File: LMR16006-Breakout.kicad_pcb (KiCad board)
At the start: 2 copper layers, 21 x 21 mm, 16 parts, among them P1 CONN_01X04, U1 LMR16006

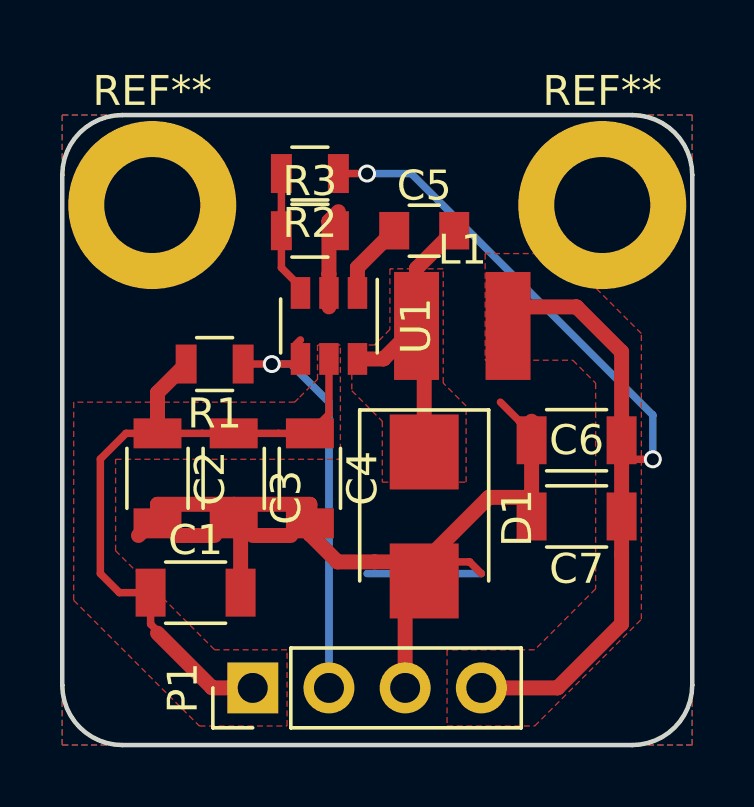
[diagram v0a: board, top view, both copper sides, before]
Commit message: added some GND vias
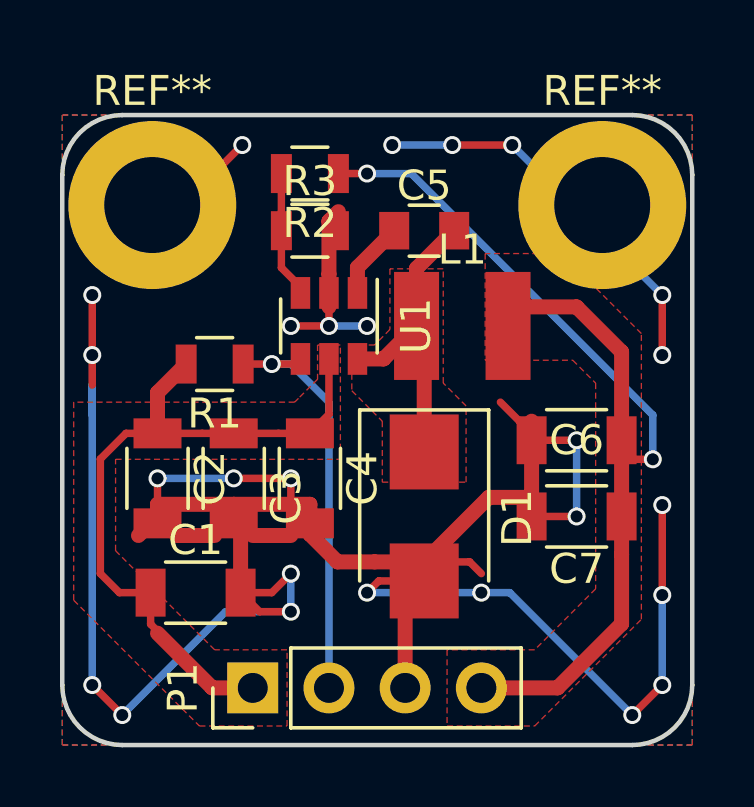
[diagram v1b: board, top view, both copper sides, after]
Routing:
- net GND: track 35.3 -> 118.3 mm, vias 0 -> 26
- net (no net): track 3.81 -> 0.00 mm
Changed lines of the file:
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@@
     (thickness 1.6)
     (drawings 8)
-    (tracks 83)
+    (tracks 147)
     (zones 0)
     (modules 16)
@@
   (gr_line (start 122 89) (end 139 89) (layer Edge.Cuts) (width 0.15))
   (gr_line (start 120 108) (end 120 91) (layer Edge.Cuts) (width 0.15))
-  (segment (start 133.97 104.285) (end 130.16 104.285) (width 0.25) (layer B.Cu) (net 0))
   (segment (start 125 108.095) (end 123.175 106.27) (width 0.5) (layer F.Cu) (net 1))
   (segment (start 122.945 104.92) (end 122.945 105.97) (width 0.25) (layer F.Cu) (net 1))
@@
   (segment (start 123.175 98.255) (end 124.13 97.3) (width 0.5) (layer F.Cu) (net 1))
   (segment (start 126.35 108.095) (end 125 108.095) (width 0.5) (layer F.Cu) (net 1))
+  (segment (start 128.89 96.03) (end 127.62 96.03) (width 0.25) (layer F.Cu) (net 2))
+  (via (at 127.62 96.03) (size 0.6) (drill 0.4) (layers F.Cu B.Cu) (net 2))
+  (segment (start 128.89 96.03) (end 130.16 96.03) (width 0.25) (layer B.Cu) (net 2))
+  (via (at 130.16 96.03) (size 0.6) (drill 0.4) (layers F.Cu B.Cu) (net 2))
+  (segment (start 128.89 94.93) (end 128.89 96.03) (width 0.25) (layer F.Cu) (net 2))
+  (via (at 128.89 96.03) (size 0.6) (drill 0.4) (layers F.Cu B.Cu) (net 2))
+  (segment (start 123 92) (end 124 92) (width 0.25) (layer F.Cu) (net 2))
+  (segment (start 124 92) (end 126 90) (width 0.25) (layer F.Cu) (net 2))
+  (via (at 126 90) (size 0.6) (drill 0.4) (layers F.Cu B.Cu) (net 2))
+  (segment (start 133 90) (end 131 90) (width 0.25) (layer B.Cu) (net 2))
+  (via (at 131 90) (size 0.6) (drill 0.4) (layers F.Cu B.Cu) (net 2))
+  (segment (start 135 90) (end 133 90) (width 0.25) (layer F.Cu) (net 2))
+  (via (at 133 90) (size 0.6) (drill 0.4) (layers F.Cu B.Cu) (net 2))
+  (segment (start 138 92) (end 137 92) (width 0.25) (layer B.Cu) (net 2))
+  (segment (start 137 92) (end 135 90) (width 0.25) (layer B.Cu) (net 2))
+  (via (at 135 90) (size 0.6) (drill 0.4) (layers F.Cu B.Cu) (net 2))
+  (segment (start 140 95) (end 140 97) (width 0.25) (layer F.Cu) (net 2))
+  (via (at 140 97) (size 0.6) (drill 0.4) (layers F.Cu B.Cu) (net 2))
+  (segment (start 138 92) (end 138 93) (width 0.25) (layer B.Cu) (net 2))
+  (via (at 140 95) (size 0.6) (drill 0.4) (layers F.Cu B.Cu) (net 2))
+  (segment (start 138 93) (end 140 95) (width 0.25) (layer B.Cu) (net 2))
+  (segment (start 140 105) (end 140 102) (width 0.25) (layer F.Cu) (net 2))
+  (via (at 140 102) (size 0.6) (drill 0.4) (layers F.Cu B.Cu) (net 2))
+  (segment (start 140 108) (end 140 105) (width 0.25) (layer B.Cu) (net 2))
+  (via (at 140 105) (size 0.6) (drill 0.4) (layers F.Cu B.Cu) (net 2))
+  (segment (start 139 109) (end 140 108) (width 0.25) (layer F.Cu) (net 2))
+  (via (at 140 108) (size 0.6) (drill 0.4) (layers F.Cu B.Cu) (net 2))
+  (segment (start 133.97 104.92) (end 134.92 104.92) (width 0.25) (layer B.Cu) (net 2))
+  (segment (start 134.92 104.92) (end 139 109) (width 0.25) (layer B.Cu) (net 2))
+  (via (at 139 109) (size 0.6) (drill 0.4) (layers F.Cu B.Cu) (net 2))
+  (segment (start 121 99) (end 121 98) (width 0.25) (layer B.Cu) (net 2))
+  (segment (start 121 108) (end 121 99) (width 0.25) (layer B.Cu) (net 2))
+  (segment (start 121 99) (end 121 97) (width 0.25) (layer B.Cu) (net 2))
+  (segment (start 121 98) (end 121 95) (width 0.25) (layer F.Cu) (net 2))
+  (via (at 121 95) (size 0.6) (drill 0.4) (layers F.Cu B.Cu) (net 2))
+  (via (at 121 97) (size 0.6) (drill 0.4) (layers F.Cu B.Cu) (net 2))
+  (via (at 122 109) (size 0.6) (drill 0.4) (layers F.Cu B.Cu) (net 2))
+  (segment (start 125.445 105.555) (end 122 109) (width 0.25) (layer B.Cu) (net 2))
+  (segment (start 127.62 105.555) (end 125.445 105.555) (width 0.25) (layer B.Cu) (net 2))
+  (via (at 121 108) (size 0.6) (drill 0.4) (layers F.Cu B.Cu) (net 2))
+  (segment (start 122 109) (end 121 108) (width 0.25) (layer F.Cu) (net 2))
+  (segment (start 137.145 99.84) (end 135.645 99.84) (width 0.25) (layer F.Cu) (net 2))
+  (segment (start 137.145 102.38) (end 137.145 99.84) (width 0.25) (layer B.Cu) (net 2))
+  (via (at 137.145 99.84) (size 0.6) (drill 0.4) (layers F.Cu B.Cu) (net 2))
+  (segment (start 135.645 102.38) (end 137.145 102.38) (width 0.25) (layer F.Cu) (net 2))
+  (via (at 137.145 102.38) (size 0.6) (drill 0.4) (layers F.Cu B.Cu) (net 2))
+  (segment (start 130.16 104.92) (end 133.97 104.92) (width 0.25) (layer B.Cu) (net 2))
+  (via (at 133.97 104.92) (size 0.6) (drill 0.4) (layers F.Cu B.Cu) (net 2))
+  (segment (start 132.065 104.53) (end 130.55 104.53) (width 0.25) (layer F.Cu) (net 2))
+  (segment (start 130.55 104.53) (end 130.16 104.92) (width 0.25) (layer F.Cu) (net 2))
+  (via (at 130.16 104.92) (size 0.6) (drill 0.4) (layers F.Cu B.Cu) (net 2))
+  (segment (start 127.62 105.555) (end 126.58 105.555) (width 0.25) (layer F.Cu) (net 2))
+  (segment (start 126.58 105.555) (end 125.945 104.92) (width 0.25) (layer F.Cu) (net 2))
+  (segment (start 127.62 104.285) (end 127.62 105.555) (width 0.25) (layer B.Cu) (net 2))
+  (via (at 127.62 105.555) (size 0.6) (drill 0.4) (layers F.Cu B.Cu) (net 2))
+  (segment (start 125.945 104.92) (end 126.985 104.92) (width 0.25) (layer F.Cu) (net 2))
+  (segment (start 126.985 104.92) (end 127.62 104.285) (width 0.25) (layer F.Cu) (net 2))
+  (via (at 127.62 104.285) (size 0.6) (drill 0.4) (layers F.Cu B.Cu) (net 2))
+  (segment (start 127.62 101.11) (end 127.62 101.975) (width 0.25) (layer F.Cu) (net 2))
+  (segment (start 127.62 101.975) (end 128.255 102.61) (width 0.25) (layer F.Cu) (net 2))
+  (segment (start 125.715 101.11) (end 127.62 101.11) (width 0.25) (layer F.Cu) (net 2))
+  (via (at 127.62 101.11) (size 0.6) (drill 0.4) (layers F.Cu B.Cu) (net 2))
+  (segment (start 123.175 101.11) (end 125.715 101.11) (width 0.25) (layer B.Cu) (net 2))
+  (via (at 125.715 101.11) (size 0.6) (drill 0.4) (layers F.Cu B.Cu) (net 2))
+  (segment (start 123.175 102.61) (end 123.175 101.11) (width 0.25) (layer F.Cu) (net 2))
+  (via (at 123.175 101.11) (size 0.6) (drill 0.4) (layers F.Cu B.Cu) (net 2))
   (segment (start 132.065 103.895) (end 133.58 103.895) (width 0.25) (layer F.Cu) (net 2))
   (segment (start 133.58 103.895) (end 133.97 104.285) (width 0.25) (layer F.Cu) (net 2))
@@
   (via (at 126.985 97.3) (size 0.6) (drill 0.4) (layers F.Cu B.Cu) (net 6))
   (segment (start 128.89 108.095) (end 128.89 98.57) (width 0.25) (layer B.Cu) (net 6))
-  (segment (start 127.77 96.665) (end 127.94 96.495) (width 0.25) (layer F.Cu) (net 6))
   (segment (start 127.305 92.855) (end 127.305 90.95) (width 0.25) (layer F.Cu) (net 7))
   (segment (start 127.305 92.855) (end 127.305 94.09) (width 0.25) (layer F.Cu) (net 7))

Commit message: some finetuning
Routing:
- net GND: track 118.3 -> 121.3 mm, vias 26 -> 28
- net VAA: track 35.4 -> 34.7 mm
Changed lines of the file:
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@@
     (thickness 1.6)
     (drawings 8)
-    (tracks 147)
+    (tracks 154)
     (zones 0)
     (modules 16)
@@
   (segment (start 123.175 98.255) (end 124.13 97.3) (width 0.5) (layer F.Cu) (net 1))
   (segment (start 126.35 108.095) (end 125 108.095) (width 0.5) (layer F.Cu) (net 1))
+  (segment (start 121 95) (end 121 97) (width 0.25) (layer F.Cu) (net 2))
+  (via (at 121 97) (size 0.6) (drill 0.4) (layers F.Cu B.Cu) (net 2))
+  (segment (start 123.175 101.11) (end 123.175 97.175) (width 0.25) (layer B.Cu) (net 2))
+  (segment (start 123.175 97.175) (end 121 95) (width 0.25) (layer B.Cu) (net 2))
+  (via (at 121 95) (size 0.6) (drill 0.4) (layers F.Cu B.Cu) (net 2))
+  (segment (start 140 101) (end 140 99) (width 0.25) (layer F.Cu) (net 2))
+  (via (at 140 99) (size 0.6) (drill 0.4) (layers F.Cu B.Cu) (net 2))
+  (segment (start 140 103) (end 140 101) (width 0.25) (layer B.Cu) (net 2))
+  (via (at 140 101) (size 0.6) (drill 0.4) (layers F.Cu B.Cu) (net 2))
+  (segment (start 140 105) (end 140 103) (width 0.25) (layer B.Cu) (net 2))
   (segment (start 128.89 96.03) (end 127.62 96.03) (width 0.25) (layer F.Cu) (net 2))
   (via (at 127.62 96.03) (size 0.6) (drill 0.4) (layers F.Cu B.Cu) (net 2))
@@
   (segment (start 138 93) (end 140 95) (width 0.25) (layer B.Cu) (net 2))
   (segment (start 140 105) (end 140 102) (width 0.25) (layer F.Cu) (net 2))
-  (via (at 140 102) (size 0.6) (drill 0.4) (layers F.Cu B.Cu) (net 2))
+  (via (at 140 103) (size 0.6) (drill 0.4) (layers F.Cu B.Cu) (net 2))
   (segment (start 140 108) (end 140 105) (width 0.25) (layer B.Cu) (net 2))
   (via (at 140 105) (size 0.6) (drill 0.4) (layers F.Cu B.Cu) (net 2))
@@
   (via (at 139 109) (size 0.6) (drill 0.4) (layers F.Cu B.Cu) (net 2))
   (segment (start 121 99) (end 121 98) (width 0.25) (layer B.Cu) (net 2))
-  (segment (start 121 108) (end 121 99) (width 0.25) (layer B.Cu) (net 2))
   (segment (start 121 99) (end 121 97) (width 0.25) (layer B.Cu) (net 2))
-  (segment (start 121 98) (end 121 95) (width 0.25) (layer F.Cu) (net 2))
-  (via (at 121 95) (size 0.6) (drill 0.4) (layers F.Cu B.Cu) (net 2))
-  (via (at 121 97) (size 0.6) (drill 0.4) (layers F.Cu B.Cu) (net 2))
   (via (at 122 109) (size 0.6) (drill 0.4) (layers F.Cu B.Cu) (net 2))
   (segment (start 125.445 105.555) (end 122 109) (width 0.25) (layer B.Cu) (net 2))
@@
   (segment (start 132.065 99.595) (end 132.065 95.65) (width 0.5) (layer F.Cu) (net 4))
   (segment (start 132.065 95.65) (end 131.81 95.395) (width 0.5) (layer F.Cu) (net 4))
-  (segment (start 131.635 90.95) (end 139.685 99) (width 0.25) (layer B.Cu) (net 5))
-  (segment (start 130.16 90.95) (end 131.635 90.95) (width 0.25) (layer B.Cu) (net 5))
+  (segment (start 131.95 90.95) (end 138.645 97.645) (width 0.25) (layer B.Cu) (net 5))
+  (segment (start 138.645 97.645) (end 138.645 99) (width 0.25) (layer B.Cu) (net 5))
+  (segment (start 130.16 90.95) (end 131.95 90.95) (width 0.25) (layer B.Cu) (net 5))
+  (segment (start 138.645 101.11) (end 138.645 99) (width 0.25) (layer B.Cu) (net 5))
+  (segment (start 138.645 101.11) (end 138.645 101.745) (width 0.5) (layer F.Cu) (net 5))
+  (segment (start 138.645 100.475) (end 138.645 101.11) (width 0.5) (layer F.Cu) (net 5))
+  (via (at 138.645 101.11) (size 0.6) (drill 0.4) (layers F.Cu B.Cu) (net 5))
   (segment (start 129.205 90.95) (end 130.16 90.95) (width 0.25) (layer F.Cu) (net 5))
   (via (at 130.16 90.95) (size 0.6) (drill 0.4) (layers F.Cu B.Cu) (net 5))
-  (segment (start 139.685 100.475) (end 139.685 99) (width 0.25) (layer B.Cu) (net 5))
-  (segment (start 138.645 100.475) (end 138.645 101.745) (width 0.5) (layer F.Cu) (net 5))
   (segment (start 138.645 99.205) (end 138.645 100.475) (width 0.5) (layer F.Cu) (net 5))
-  (segment (start 138.645 100.475) (end 139.685 100.475) (width 0.25) (layer F.Cu) (net 5))
-  (via (at 139.685 100.475) (size 0.6) (drill 0.4) (layers F.Cu B.Cu) (net 5))
   (segment (start 138.645 103.65) (end 138.645 101.745) (width 0.5) (layer F.Cu) (net 5))
   (segment (start 138.645 105.96) (end 138.645 103.65) (width 0.5) (layer F.Cu) (net 5))
@@
     (polygon
       (pts
-        (xy 134.097 93.617) (xy 134.097 97.173) (xy 137.018 97.173) (xy 137.78 97.935) (xy 137.78 104.793)
-        (xy 135.748 106.825) (xy 132.827 106.825) (xy 132.827 109.365) (xy 135.748 109.365) (xy 139.304 105.809)
-        (xy 139.304 96.284) (xy 137.653 94.633) (xy 136.51 93.617)
+        (xy 134.097 94.252) (xy 134.097 97.808) (xy 137.018 97.808) (xy 137.78 98.57) (xy 137.78 104.793)
+        (xy 135.748 106.825) (xy 132.827 106.825) (xy 132.827 109.365) (xy 135.748 109.365) (xy 139.431 105.682)
+        (xy 139.431 97.046) (xy 137.526 95.141) (xy 136.637 95.141) (xy 135.621 94.252)
       )
     )
